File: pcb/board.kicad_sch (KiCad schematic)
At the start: 4 parts

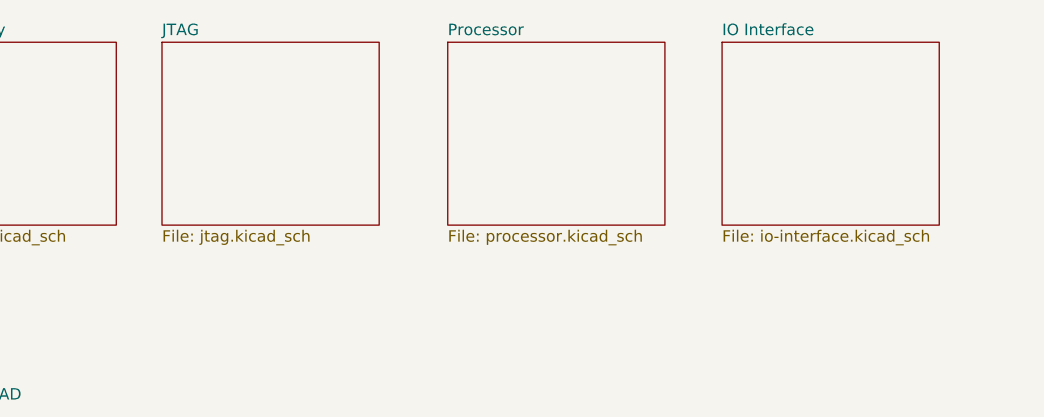
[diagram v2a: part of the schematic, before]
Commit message: add the usb to spi interface
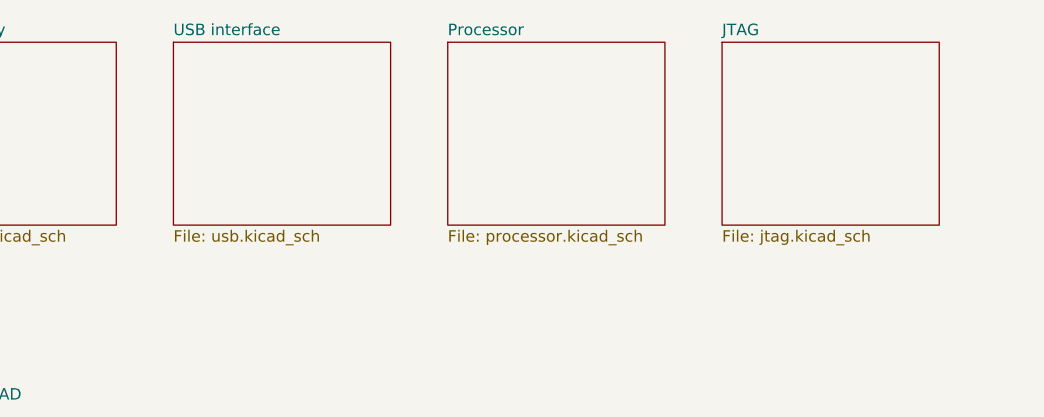
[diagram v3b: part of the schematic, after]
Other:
- removed sheet IO Interface
- added sheet USB interface (usb.kicad_sch)
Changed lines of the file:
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@@
     (stroke (width 0.0006) (type solid) (color 0 0 0 0))
     (fill (color 0 0 0 0.0000))
-    (property "Sheet name" "IO Interface" (id 0) (at 124.46 24.7643 0)
+    (property "Sheet name" "JTAG" (id 0) (at 124.46 24.7643 0)
       (effects (font (size 1.27 1.27)) (justify left bottom))
     )
-    (property "Sheet file" "io-interface.kicad_sch" (id 1) (at 124.46 46.2287 0)
-      (effects (font (size 1.27 1.27)) (justify left top))
-    )
-  )
-  (sheet (at 62.23 25.4) (size 24.13 20.32) (fields_autoplaced)
-    (stroke (width 0.0006) (type solid) (color 0 0 0 0))
-    (fill (color 0 0 0 0.0000))
-    (property "Sheet name" "JTAG" (id 0) (at 62.23 24.7643 0)
-      (effects (font (size 1.27 1.27)) (justify left bottom))
-    )
-    (property "Sheet file" "jtag.kicad_sch" (id 1) (at 62.23 46.2287 0)
+    (property "Sheet file" "jtag.kicad_sch" (id 1) (at 124.46 46.2287 0)
       (effects (font (size 1.27 1.27)) (justify left top))
     )
@@
     )
   )
+  (sheet (at 63.5 25.4) (size 24.13 20.32) (fields_autoplaced)
+    (stroke (width 0.0006) (type solid) (color 0 0 0 0))
+    (fill (color 0 0 0 0.0000))
+    (property "Sheet name" "USB interface" (id 0) (at 63.5 24.7643 0)
+      (effects (font (size 1.27 1.27)) (justify left bottom))
+    )
+    (property "Sheet file" "usb.kicad_sch" (id 1) (at 63.5 46.2287 0)
+      (effects (font (size 1.27 1.27)) (justify left top))
+    )
+  )
   (sheet_instances
     (path "/" (page "1"))
     (path "/c036d866-c247-4a79-8c95-1926a9c8f9b9/" (page "2"))
-    (path "/8ac5cdc4-b102-45f3-8410-9d92d6267eb3/" (page "3"))
     (path "/82fcb530-a5b5-40a4-adf5-fce5b9ae2e58/" (page "4"))
     (path "/deae845a-ed89-4dc8-b611-a45627046b99/" (page "5"))
+    (path "/f783d73c-35cd-4718-afa1-f83ec8c78fac/" (page "6"))
   )
   (symbol_instances
@@
       (reference "#PWR?") (unit 1) (value "GND") (footprint "")
     )
-    (path "/82fcb530-a5b5-40a4-adf5-fce5b9ae2e58/15264069-f8fa-4707-946c-4e34b6142464"
-      (reference "#PWR?") (unit 1) (value "GND") (footprint "")
-    )
     (path "/82fcb530-a5b5-40a4-adf5-fce5b9ae2e58/155bef4b-1154-4a99-b969-28e48d8c85f9"
       (reference "#PWR?") (unit 1) (value "GND") (footprint "")
     )
-    (path "/82fcb530-a5b5-40a4-adf5-fce5b9ae2e58/15b82018-fbfc-4b5f-af29-f4e820d61def"
-      (reference "#PWR?") (unit 1) (value "+3.3V") (footprint "")
-    )
     (path "/82fcb530-a5b5-40a4-adf5-fce5b9ae2e58/16589e30-21a1-4563-ba8f-91c11630dec9"
       (reference "#PWR?") (unit 1) (value "GND") (footprint "")
@@
       (reference "#PWR?") (unit 1) (value "GND") (footprint "")
     )
-    (path "/82fcb530-a5b5-40a4-adf5-fce5b9ae2e58/24725e17-6a20-43c7-be11-ccd129dd2aaa"
-      (reference "#PWR?") (unit 1) (value "GND") (footprint "")
-    )
-    (path "/82fcb530-a5b5-40a4-adf5-fce5b9ae2e58/2a36c3ac-2e8c-4994-81c0-a6bf9ef7e98e"
-      (reference "#PWR?") (unit 1) (value "GND") (footprint "")
-    )
     (path "/82fcb530-a5b5-40a4-adf5-fce5b9ae2e58/33924d65-fcc0-4be3-a624-0ee128e51d38"
       (reference "#PWR?") (unit 1) (value "GND") (footprint "")
@@
       (reference "#PWR?") (unit 1) (value "GND") (footprint "")
     )
-    (path "/82fcb530-a5b5-40a4-adf5-fce5b9ae2e58/3f206c52-b08f-4f58-89ba-65cf18ae7ac3"
-      (reference "#PWR?") (unit 1) (value "GND") (footprint "")
-    )
     (path "/82fcb530-a5b5-40a4-adf5-fce5b9ae2e58/45823650-217c-43e6-8073-6eaebc3504dc"
       (reference "#PWR?") (unit 1) (value "+3.3V") (footprint "")
     )
+    (path "/82fcb530-a5b5-40a4-adf5-fce5b9ae2e58/4619187b-2d26-4350-a101-6ef6d696acb5"
+      (reference "#PWR?") (unit 1) (value "+3.3V") (footprint "")
+    )
     (path "/82fcb530-a5b5-40a4-adf5-fce5b9ae2e58/4dca7a29-8950-4d3d-af19-672b189777ee"
       (reference "#PWR?") (unit 1) (value "GND") (footprint "")
@@
       (reference "#PWR?") (unit 1) (value "GND") (footprint "")
     )
+    (path "/82fcb530-a5b5-40a4-adf5-fce5b9ae2e58/60720f17-e556-4ad7-b1bf-4134889083e9"
+      (reference "#PWR?") (unit 1) (value "GND") (footprint "")
+    )
     (path "/82fcb530-a5b5-40a4-adf5-fce5b9ae2e58/66ae3a47-b6ee-494d-958c-7992f03b8c54"
       (reference "#PWR?") (unit 1) (value "+3.3V") (footprint "")
     )
-    (path "/82fcb530-a5b5-40a4-adf5-fce5b9ae2e58/67f634d3-0088-4ba0-88e4-c6489a5dd8eb"
-      (reference "#PWR?") (unit 1) (value "GND") (footprint "")
-    )
     (path "/82fcb530-a5b5-40a4-adf5-fce5b9ae2e58/6d858f4d-f650-4f32-8213-d334ee04d624"
       (reference "#PWR?") (unit 1) (value "GND") (footprint "")
@@
       (reference "#PWR?") (unit 1) (value "GND") (footprint "")
     )
-    (path "/82fcb530-a5b5-40a4-adf5-fce5b9ae2e58/8dfd4688-0877-474b-94ca-3c692514b200"
-      (reference "#PWR?") (unit 1) (value "+3.3V") (footprint "")
-    )
     (path "/82fcb530-a5b5-40a4-adf5-fce5b9ae2e58/b4062198-81cf-48c4-be23-e4cde525ab2c"
       (reference "#PWR?") (unit 1) (value "GND") (footprint "")
@@
       (reference "#PWR?") (unit 1) (value "+3.3V") (footprint "")
     )
-    (path "/82fcb530-a5b5-40a4-adf5-fce5b9ae2e58/d601d3c9-d1b6-4e73-967e-c8a680d30eb0"
-      (reference "#PWR?") (unit 1) (value "GND") (footprint "")
-    )
     (path "/82fcb530-a5b5-40a4-adf5-fce5b9ae2e58/d74acc11-961a-479a-badb-a0e0398e5dce"
       (reference "#PWR?") (unit 1) (value "+3.3V") (footprint "")
     )
-    (path "/82fcb530-a5b5-40a4-adf5-fce5b9ae2e58/e649c58b-ac20-40bb-8f11-cf0c12927385"
-      (reference "#PWR?") (unit 1) (value "+3.3V") (footprint "")
-    )
     (path "/82fcb530-a5b5-40a4-adf5-fce5b9ae2e58/edc3912d-0746-4589-a21e-80ff4b3a4f49"
       (reference "#PWR?") (unit 1) (value "+3.3V") (footprint "")
@@
       (reference "#PWR?") (unit 1) (value "+3.3V") (footprint "")
     )
-    (path "/82fcb530-a5b5-40a4-adf5-fce5b9ae2e58/f1ceac28-0f16-4844-84e1-9779fd0322bb"
-      (reference "#PWR?") (unit 1) (value "+3.3V") (footprint "")
+    (path "/82fcb530-a5b5-40a4-adf5-fce5b9ae2e58/0214cfc7-9780-4667-96f3-d6e5bbd19a55"
+      (reference "C?") (unit 1) (value "0.1u") (footprint "")
     )
     (path "/82fcb530-a5b5-40a4-adf5-fce5b9ae2e58/0caad7e1-6eb3-41f4-b3f9-6f1d5d37cf41"
@@
       (reference "C?") (unit 1) (value "0.1u") (footprint "")
     )
-    (path "/82fcb530-a5b5-40a4-adf5-fce5b9ae2e58/1df52785-007f-4b80-a93f-bf323aedd136"
-      (reference "C?") (unit 1) (value "100p") (footprint "")
-    )
     (path "/82fcb530-a5b5-40a4-adf5-fce5b9ae2e58/26d6fcdd-aad6-40d2-94a4-e00b8c41d6c0"
       (reference "C?") (unit 1) (value "0.1u") (footprint "")
@@
       (reference "C?") (unit 1) (value "4.7u") (footprint "")
     )
-    (path "/82fcb530-a5b5-40a4-adf5-fce5b9ae2e58/e4b208fd-2c80-434b-b576-cce958d0ca6b"
-      (reference "C?") (unit 1) (value "0.1u") (footprint "")
-    )
     (path "/82fcb530-a5b5-40a4-adf5-fce5b9ae2e58/f09e9051-b00a-4497-adcf-3856e9fb7c88"
       (reference "C?") (unit 1) (value "0.1u") (footprint "")
@@
       (reference "J?") (unit 1) (value "USB_B") (footprint "")
     )
-    (path "/82fcb530-a5b5-40a4-adf5-fce5b9ae2e58/5f917dfe-e355-46dd-9191-0c947341d377"
-      (reference "J?") (unit 1) (value "Conn_02x03_Counter_Clockwise") (footprint "")
-    )
     (path "/82fcb530-a5b5-40a4-adf5-fce5b9ae2e58/0bdf9a22-0964-40ad-997c-2adb57b33424"
       (reference "R?") (unit 1) (value "2k") (footprint "")
@@
       (reference "R?") (unit 1) (value "12k/1%") (footprint "")
     )
-    (path "/82fcb530-a5b5-40a4-adf5-fce5b9ae2e58/2299b530-047e-4e8d-b1ef-753421702446"
-      (reference "R?") (unit 1) (value "10k") (footprint "")
-    )
     (path "/82fcb530-a5b5-40a4-adf5-fce5b9ae2e58/5d21b951-29e5-4e94-b23b-674f7d802b0b"
-      (reference "R?") (unit 1) (value "10k") (footprint "")
-    )
-    (path "/82fcb530-a5b5-40a4-adf5-fce5b9ae2e58/5fb66e2d-2f38-4857-a3af-be6b271a1a31"
-      (reference "R?") (unit 1) (value "68") (footprint "")
-    )
-    (path "/82fcb530-a5b5-40a4-adf5-fce5b9ae2e58/79873d48-e0da-4475-80b5-a61bf3c14114"
-      (reference "R?") (unit 1) (value "10k") (footprint "")
-    )
-    (path "/82fcb530-a5b5-40a4-adf5-fce5b9ae2e58/7fabc52c-eca9-43f3-9c58-c922f074cb10"
-      (reference "R?") (unit 1) (value "10k") (footprint "")
-    )
-    (path "/82fcb530-a5b5-40a4-adf5-fce5b9ae2e58/9fe12b69-e947-4eb6-b1a1-12e9c53dd165"
       (reference "R?") (unit 1) (value "10k") (footprint "")
     )
@@
       (reference "U?") (unit 1) (value "FT232H") (footprint "")
     )
-    (path "/82fcb530-a5b5-40a4-adf5-fce5b9ae2e58/607212dc-3642-43a0-beb7-12d4935f025d"
-      (reference "U?") (unit 1) (value "SN74AVC4T245PW") (footprint "Package_SO:TSSOP-16_4.4x5mm_P0.65mm")
-    )
-    (path "/82fcb530-a5b5-40a4-adf5-fce5b9ae2e58/ae331ab9-18b3-4887-8388-50c15eef131d"
-      (reference "U?") (unit 1) (value "74LVC1G04") (footprint "")
-    )
     (path "/82fcb530-a5b5-40a4-adf5-fce5b9ae2e58/eb629262-9730-4b0f-b3e0-d582bc48f7aa"
       (reference "U?") (unit 1) (value "93LCxxBxxOT") (footprint "Package_TO_SOT_SMD:SOT-23-6")
     )
+    (path "/82fcb530-a5b5-40a4-adf5-fce5b9ae2e58/fa156564-09c6-459c-a95d-a9eadd119b1c"
+      (reference "U?") (unit 1) (value "SN74AVC8T245PW") (footprint "Package_SO:TSSOP-24_4.4x7.8mm_P0.65mm")
+    )
     (path "/82fcb530-a5b5-40a4-adf5-fce5b9ae2e58/5a16af7e-d5cb-4df9-8c1b-40ab464968d8"
       (reference "Y?") (unit 1) (value "12MHz") (footprint "")
@@
       (reference "U?") (unit 1) (value "TPS541620") (footprint "")
     )
-  )
+    (path "/f783d73c-35cd-4718-afa1-f83ec8c78fac/098cc34b-f8ec-4785-a2ec-4d18dcbcdafc"
+      (reference "#PWR?") (unit 1) (value "+3.3V") (footprint "")
+    )
+    (path "/f783d73c-35cd-4718-afa1-f83ec8c78fac/47faeaa2-e922-4043-ae57-f3a68cdca289"
+      (reference "#PWR?") (unit 1) (value "GND") (footprint "")
+    )
+    (path "/f783d73c-35cd-4718-afa1-f83ec8c78fac/59500ab3-90ab-4d02-b00c-f981a6458792"
+      (reference "J?") (unit 1) (value "Conn_02x03_Counter_Clockwise") (footprint "")
+    )
+  )

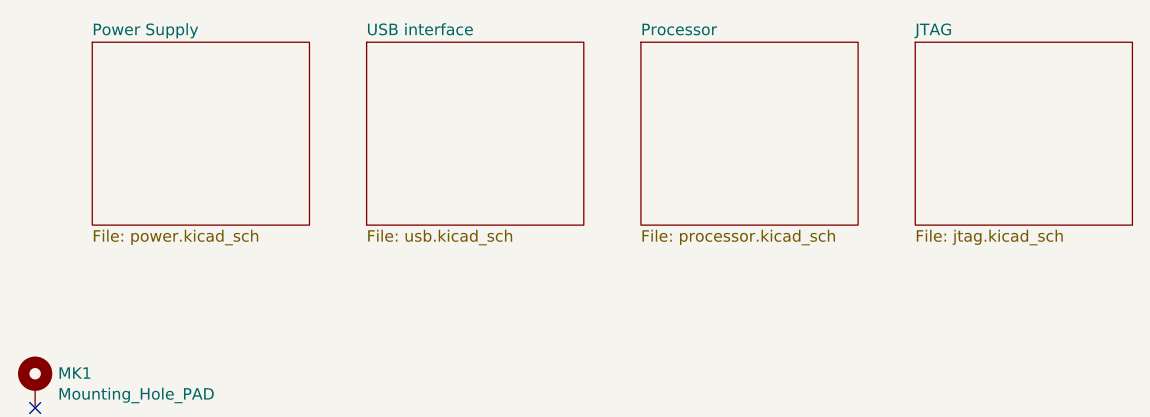
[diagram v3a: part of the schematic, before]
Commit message: add both usb to jtag and usb to spi interface
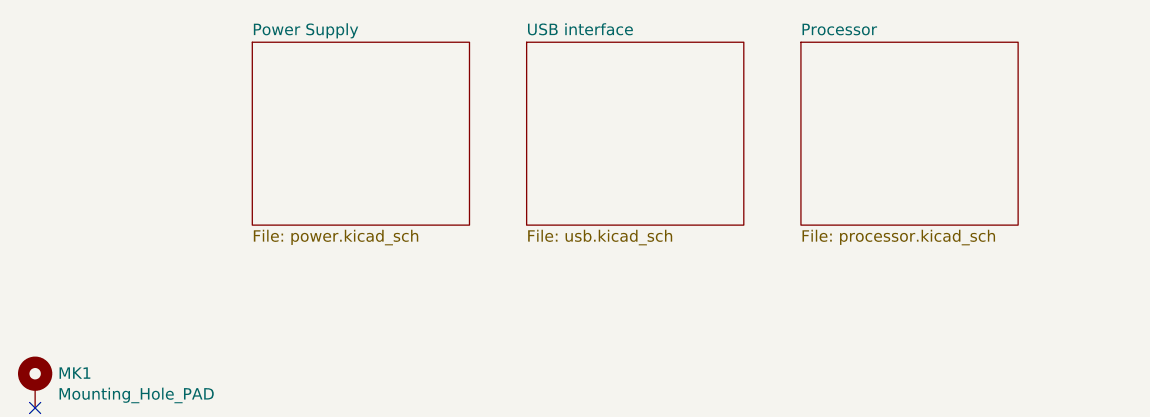
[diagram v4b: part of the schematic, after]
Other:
- removed sheet JTAG

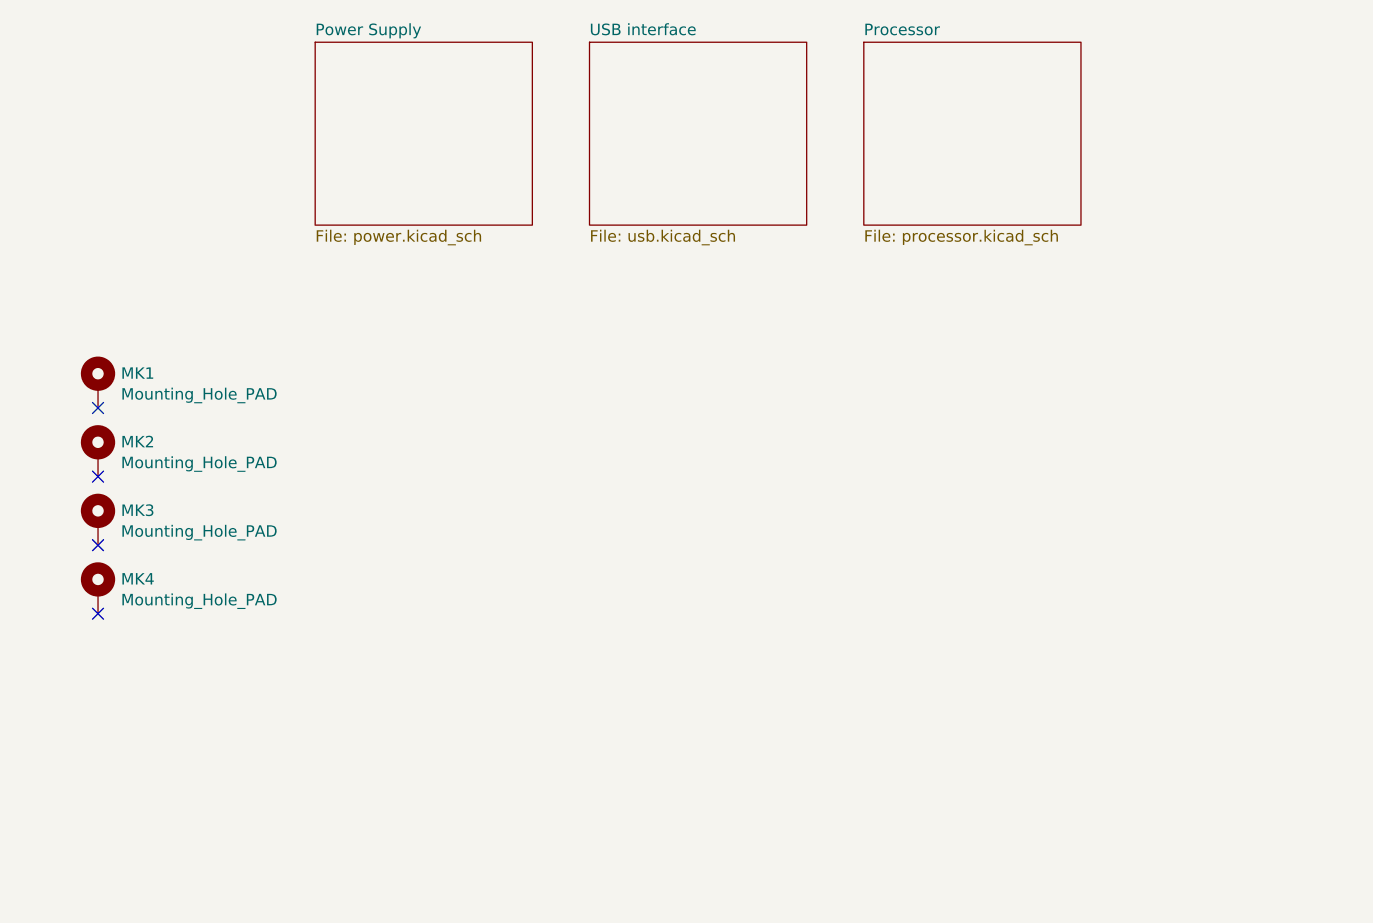
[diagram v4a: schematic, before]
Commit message: start adding processor fpga
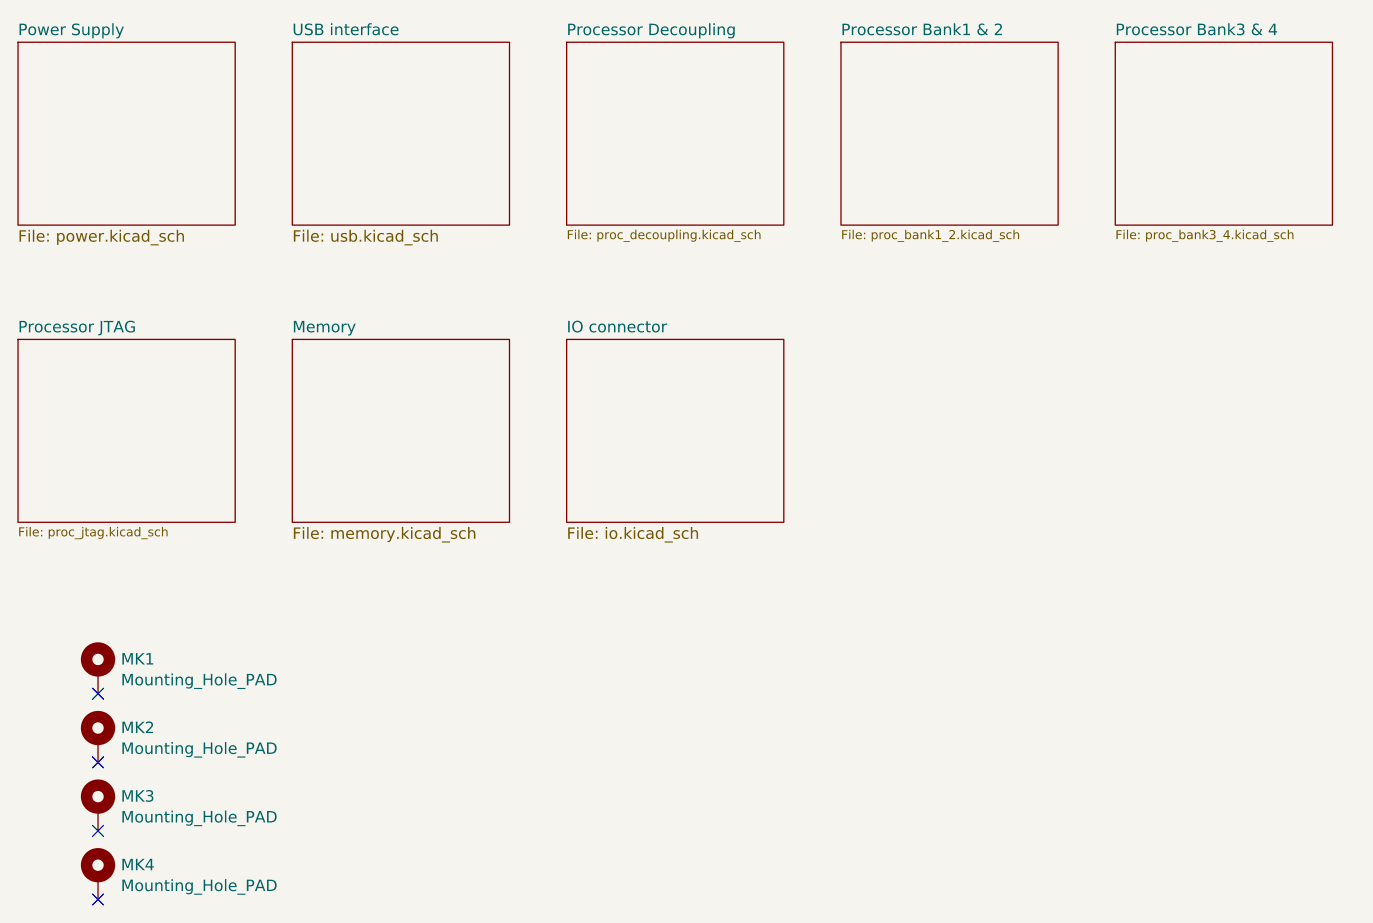
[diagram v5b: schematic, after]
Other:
- sheet Processor renamed Processor Decoupling
- added sheet IO connector (io.kicad_sch)
- added sheet Memory (memory.kicad_sch)
- added sheet Processor Bank1 & 2 (proc_bank1_2.kicad_sch)
- added sheet Processor Bank3 & 4 (proc_bank3_4.kicad_sch)
- added sheet Processor JTAG (proc_jtag.kicad_sch)
- sheet Processor Decoupling: file processor.kicad_sch -> proc_decoupling.kicad_sch
- moved on the sheet: MK1, MK2, MK3, MK4

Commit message: add flash memory
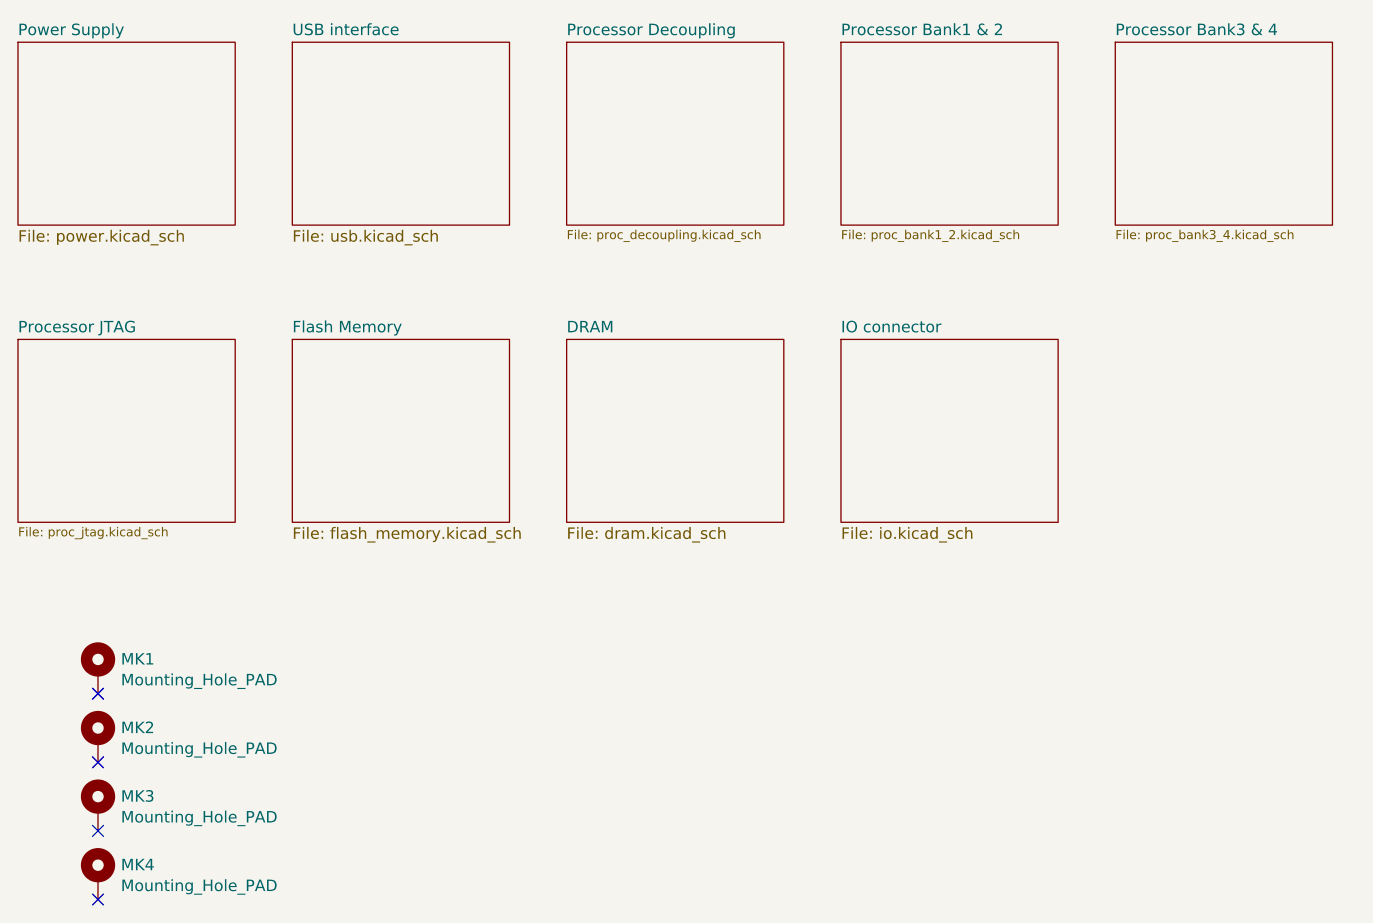
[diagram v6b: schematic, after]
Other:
- sheet Memory renamed Flash Memory
- added sheet DRAM (dram.kicad_sch)
- sheet Flash Memory: file memory.kicad_sch -> flash_memory.kicad_sch
